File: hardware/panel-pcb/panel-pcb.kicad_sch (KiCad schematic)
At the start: 0 parts

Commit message: Panel PCB schematic: RP2040 core, flash, USB-C, power-in, RS-485
- RP2040 core: decoupling, ADC_AVDD filter, crystal, RUN, TESTEN, SWD header,
  values sourced from TI's official RP2040 hardware design guide
- W25Q32JV flash with BOOTSEL pushbutton (button instead of the guide's jumper,
  matching Pico's approach)
- USB-C connector (16-pin USB2.0-only), CC pull-downs, D+/D- series resistors,
  plus a VBUS/12V power-OR so the panel can be flashed and bench-tested over
  USB alone with 12V absent
- Power-in: 12V bus connectors, AMS1117-5.0 -> AMS1117-3.3 LDO cascade
- RS-485: THVD1419 transceiver, bused IN/OUT connectors, DPDT slide switch for
  termination (one pole gates the 120 ohm resistor, the other reports switch
  state to the RP2040 so termination state is always known)
- 3-bit player/pad ID DIP switch added to the master MCU spec, replacing
  stock SMX's jumper-based P1/P2 selection
- Panel PCB physical measurements replaced with real caliper measurements
  (mounting holes, LED lattice pitch, connector positions, board outline)
  from a pulled Gen5 panel, superseding the earlier photo-based estimates
- Preferred USB-C mounting style set to vertical DIP through-hole
- Reference photos of the stock panel PCB added under images/
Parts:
- added C1, C2: 15pF, Capacitor_SMD:C_0603_1608Metric, symbol Device:C
- added C10, C11, C12, C13, C15, C20, C5, C6, C7, C8, C9: 100nF, Capacitor_SMD:C_0603_1608Metric, symbol Device:C
- added C14, C4: 1uF, Capacitor_SMD:C_0603_1608Metric, symbol Device:C
- added C16, C18: 10uF, Capacitor_THT:CP_Radial_D6.3mm_P2.50mm, symbol Device:C
- added C17, C19: 22uF, Capacitor_THT:CP_Radial_D6.3mm_P2.50mm, symbol Device:C
- added C3: 2.2uF, Capacitor_SMD:C_0603_1608Metric, symbol Device:C
- added D1, D2: Schottky, Diode_SMD:D_SOD-123, symbol Device:D_Schottky
- added J1: SWD, Connector_PinHeader_2.54mm:PinHeader_1x03_P2.54mm_Vertical, symbol Connector_Generic:Conn_01x03
- added J2: USB_C_Receptacle_USB2.0_16P, symbol Connector:USB_C_Receptacle_USB2.0_16P
- added J3: 12V_IN, symbol Connector_Generic:Conn_01x02
- added J4: 12V_OUT, symbol Connector_Generic:Conn_01x02
- added J5: RS-485 IN, symbol Connector_Generic:Conn_01x03
- added J6: RS-485 OUT, symbol Connector_Generic:Conn_01x03
- added R1: 201R 1%, Resistor_SMD:R_0603_1608Metric, symbol Device:R
- added R10: 120, Resistor_SMD:R_0603_1608Metric, symbol Device:R
- added R2: 10k, Resistor_SMD:R_0603_1608Metric, symbol Device:R
- added R3: 1k 1%, Resistor_SMD:R_0603_1608Metric, symbol Device:R
- added R4: 1k, Resistor_SMD:R_0603_1608Metric, symbol Device:R
- added R5: 10k DNF, Resistor_SMD:R_0603_1608Metric, symbol Device:R
- added R6, R7: 27R 1%, Resistor_SMD:R_0603_1608Metric, symbol Device:R
- added R8, R9: 5.1k, Resistor_SMD:R_0603_1608Metric, symbol Device:R
- added SW1: BOOTSEL, Button_Switch_SMD:SW_SPST_B3U-1000P, symbol Switch:SW_Push
- added SW2: RS-485 Termination, symbol Switch:SW_Slide_DPDT
- added TP1: RUN, TestPoint:TestPoint_Pad_1.5x1.5mm, symbol Connector:TestPoint
- added U1: RP2040, Package_DFN_QFN:QFN-56-1EP_7x7mm_P0.4mm_EP3.2x3.2mm, symbol MCU_RaspberryPi:RP2040
- added U2: W25Q32JV, Package_SO:SOIC-8_5.3x5.3mm_P1.27mm, symbol Memory_Flash:W25Q32JVSS
- added U3: AMS1117-5.0, Package_TO_SOT_SMD:SOT-223-3_TabPin2, symbol Regulator_Linear:AMS1117-5.0
- added U4: AMS1117-3.3, Package_TO_SOT_SMD:SOT-223-3_TabPin2, symbol Regulator_Linear:AMS1117-3.3
- added U5: THVD1419, Package_SO:SOIC-8_3.9x4.9mm_P1.27mm, symbol Interface_UART:THVD1420D
- added X1: 12MHz, Crystal:Crystal_SMD_3225-4Pin_3.2x2.5mm, symbol Device:Crystal_GND24
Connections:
- new net: C2.1, R3.1, X1.3
- new net: J1.3 (Pin_3), U1.24 (SWCLK)
- new net: J1.1 (Pin_1), U1.25 (SWDIO)
- new net: R2.2, TP1.1, U1.26 (RUN)
- new net: C3.2, R1.2, U1.43 (ADC_AVDD)
- new net: R7.2, U1.46 (USB_DM)
- new net: R6.1, U1.47 (USB_DP)
- new net: J2.B5 (CC2), R9.1
- new net: J2.A5 (CC1), R8.2
- new net: C17.1, D2.2 (A), U3.2 (VO)
- new net: R10.2, SW2.1 (A)
- new net +1.1V: C12.1, C13.1, C4.1, U1.23 (DVDD), U1.45 (VREG_VOUT), U1.50 (DVDD)
- new net +12.0V: C16.1, J3.1 (Pin_1), J4.1 (Pin_1), U3.3 (VI)
- new net +3V3: C10.1, C11.1, C14.2, C15.1, C19.1, C20.1, C5.1, C6.1, C7.1, C8.1, C9.1, R1.1, R2.1, R5.1, U1.1 (IOVDD), U1.10 (IOVDD), U1.22 (IOVDD), U1.33 (IOVDD), U1.42 (IOVDD), U1.44 (VREG_VIN), U1.48 (USB_VDD), U1.49 (IOVDD), U2.8 (VCC), U4.2 (VO), U5.8 (VCC)
- new net +5.0V: C18.1, D1.1 (K), D2.1 (K), U4.3 (VI)
- new net GND: C1.2, C10.2, C11.2, C12.2, C13.2, C14.1, C15.2, C16.2, C17.2, C18.2, C19.2, C2.2, C20.2, C3.1, C4.2, C5.2, C6.2, C7.2, C8.2, C9.2, J1.2 (Pin_2), J2.A1 (GND), J2.A12 (GND), J2.B1 (GND), J2.B12 (GND), J2.SH (SHIELD), J3.2 (Pin_2), J4.2 (Pin_2), R8.1, R9.2, SW1.2, SW2.6 (C), U1.19 (TESTEN), U1.57 (GND), U2.4 (GND), U3.1 (GND), U4.1 (GND), U5.5 (GND), X1.2 (G), X1.4 (G)
- new net GPIO0: U1.2 (GPIO0), U5.4 (DI)
- new net GPIO1: U1.3 (GPIO1), U5.1 (RO)
- new net GPIO10: SW2.5 (B), U1.13 (GPIO10)
- new net GPIO11: U1.14 (GPIO11)
- new net GPIO12: U1.15 (GPIO12)
- new net GPIO13: U1.16 (GPIO13)
- new net GPIO14: U1.17 (GPIO14)
- new net GPIO15: U1.18 (GPIO15)
- new net GPIO16: U1.27 (GPIO16)
- new net GPIO17: U1.28 (GPIO17)
- new net GPIO18: U1.29 (GPIO18)
- new net GPIO19: U1.30 (GPIO19)
- new net GPIO2: U1.4 (GPIO2), U5.2 (~{RE}), U5.3 (DE)
- new net GPIO20: U1.31 (GPIO20)
- new net GPIO21: U1.32 (GPIO21)
- new net GPIO22: U1.34 (GPIO22)
- new net GPIO23: U1.35 (GPIO23)
- new net GPIO24: U1.36 (GPIO24)
- new net GPIO25: U1.37 (GPIO25)
- new net GPIO26/ADC0: U1.38 (GPIO26/ADC0)
- new net GPIO27/ADC1: U1.39 (GPIO27/ADC1)
- new net GPIO28/ADC2: U1.40 (GPIO28/ADC2)
- new net GPIO29/ADC3: U1.41 (GPIO29/ADC3)
- new net GPIO3: U1.5 (GPIO3)
- new net GPIO4: U1.6 (GPIO4)
- new net GPIO5: U1.7 (GPIO5)
- new net GPIO6: U1.8 (GPIO6)
- new net GPIO7: U1.9 (GPIO7)
- new net GPIO8: U1.11 (GPIO8)
- new net GPIO9: U1.12 (GPIO9)
- new net QSPI_SCLK: U1.52 (QSPI_SCLK), U2.6 (CLK)
- new net QSPI_SD0: U1.53 (QSPI_SD0), U2.5 (DI/IO_{0})
- new net QSPI_SD1: U1.55 (QSPI_SD1), U2.2 (DO/IO_{1})
- new net QSPI_SD2: U1.54 (QSPI_SD2), U2.3 (~{WP}/IO_{2})
- new net QSPI_SD3: U1.51 (QSPI_SD3), U2.7 (~{HOLD}/~{RESET}/IO_{3})
- new net QSPI_SS: R4.2, R5.2, U1.56 (~{QSPI_SS}), U2.1 (~{CS})
- new net RS485_A: J5.1 (Pin_1), J6.1 (Pin_1), SW2.2 (B), U5.6 (A)
- new net RS485_B: J5.2 (Pin_2), J6.2 (Pin_2), R10.1, U5.7 (B)
- new net USB_BOOT: R4.1, SW1.1
- new net USB_DM: J2.A7 (D-), J2.B7 (D-), R7.1
- new net USB_DP: J2.A6 (D+), J2.B6 (D+), R6.2
- new net VBUS: D1.2 (A), J2.A4 (VBUS), J2.A9 (VBUS), J2.B4 (VBUS), J2.B9 (VBUS)
- new net XIN: C1.1, U1.20 (XIN), X1.1
- new net XOUT: R3.2, U1.21 (XOUT)
- no-connect marks 0 -> 6
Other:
- note added: "12v Power"
- note added: "3v3 Power"
- note added: "5v Power"
- note added: "Buttons"
- note added: "Close to ADC_AVDD pin"
- note added: "Each close to a DVDD pin"
- note added: "Each close to an IOVDD pin"
- note added: "Microcontroller"
- note added: "QSPI Flash"
- note added: "RS-485"
- note added: "USB"

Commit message: Panel PCB schematic complete: FSR, LED chain, INT, ID DIP + doc updates
- FSR inputs x4 (J7-J10, 10k dividers, 10nF C0G ADC caps)
- LED chain: 25x WS2815 + SN74AHCT125 shifter, GPIO3 debug LED (optional populate)
- WS2815 per-LED 100nF corrected to VCC->GND per datasheet (BOM.md note fixed)
- INT out (100R series + single-pos terminal), 4-pos panel ID DIP
- Spare shifter gates: inputs + ~OE grounded, outputs no-connect
- Debug press LED gated to diagnostic modes 9-13 (docs/PANEL_CONFIG.md)

ERC clean, netlist-verified pin-exact (~330 parts).
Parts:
- added C21, C22, C23, C24: 10nF C0G, symbol Device:C
- added C25, C26, C27, C28, C29, C30, C31, C32, C33, C34, C35, C36, C37, C38, C39, C40, C41, C42, C43, C44, C45, C46, C47, C48, C49, C50: 100nF, symbol Device:C
- added D10, D11, D12, D13, D14, D15, D16, D17, D18, D19, D20, D21, D22, D23, D24, D25, D26, D27, D3, D4, D5, D6, D7, D8, D9: WS2815, symbol LED:WS2813
- added D28: DEBUG, symbol Device:LED
- added J10: FSR West, symbol Connector_Generic:Conn_01x02
- added J11: INT OUT, symbol Connector_Generic:Conn_01x01
- added J7: FSR North, symbol Connector_Generic:Conn_01x02
- added J8: FSR East, symbol Connector_Generic:Conn_01x02
- added J9: FSR South, symbol Connector_Generic:Conn_01x02
- added R11, R12, R13, R14: 10k, symbol Device:R
- added R15: 100R, symbol Device:R
- added R16: 330R, symbol Device:R
- added R17: 1k, symbol Device:R
- added SW3: PANEL_ID, symbol Switch:SW_DIP_x04
- added U6: SN74AHCT125, symbol 74xx:74AHCT125
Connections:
- net +12.0V: now also D10.2 (VDD), D11.2 (VDD), D12.2 (VDD), D13.2 (VDD), D14.2 (VDD), D15.2 (VDD), D16.2 (VDD), D17.2 (VDD), D18.2 (VDD), D19.2 (VDD), D20.2 (VDD), D21.2 (VDD), D22.2 (VDD), D23.2 (VDD), D24.2 (VDD), D25.2 (VDD), D26.2 (VDD), D27.2 (VDD), D3.2 (VDD), D4.2 (VDD), D5.2 (VDD), D6.2 (VDD), D7.2 (VDD), D8.2 (VDD), D9.2 (VDD)
- net +3V3: now also J10.2 (Pin_2), J7.2 (Pin_2), J8.2 (Pin_2), J9.2 (Pin_2)
- net +5.0V: now also C50.1, U6.14 (VCC)
- net GND: now also C21.2, C22.2, C23.2, C24.2, C25.2, C26.2, C27.2, C28.2, C29.2, C30.2, C31.2, C32.2, C33.2, C34.2, C35.2, C36.2, C37.2, C38.2, C39.2, C40.2, C41.2, C42.2, C43.2, C44.2, C45.2, C46.2, C47.2, C48.2, C49.2, C50.2, D10.5 (GND), D11.5 (GND), D12.5 (GND), D13.5 (GND), D14.5 (GND), D15.5 (GND), D16.5 (GND), D17.5 (GND), D18.5 (GND), D19.5 (GND), D20.5 (GND), D21.5 (GND), D22.5 (GND), D23.5 (GND), D24.5 (GND), D25.5 (GND), D26.5 (GND), D27.5 (GND), D28.1 (K), D3.5 (GND), D4.5 (GND), D5.5 (GND), D6.5 (GND), D7.5 (GND), D8.5 (GND), D9.5 (GND), R11.2, R12.2, R13.2, R14.2, SW3.5, SW3.6, SW3.7, SW3.8, U6.1, U6.10, U6.12, U6.13, U6.4, U6.5, U6.7 (GND), U6.9
- net GPIO16: now also U6.2
- net GPIO26/ADC0: now also C21.1, J7.1 (Pin_1), R11.1
- net GPIO27/ADC1: now also C22.1, J8.1 (Pin_1), R12.1
- net GPIO28/ADC2: now also C23.1, J9.1 (Pin_1), R13.1
- net GPIO29/ADC3: now also C24.1, J10.1 (Pin_1), R14.1
- net GPIO3: now also R17.1
- net GPIO5: now also R15.1
- net GPIO6: now also SW3.1
- net GPIO7: now also SW3.2
- net GPIO8: now also SW3.3
- net GPIO9: now also SW3.4
- new net: C44.1, D22.1 (VCC)
- new net: C41.1, D19.1 (VCC)
- new net: C28.1, D6.1 (VCC)
- new net: C32.1, D10.1 (VCC)
- new net: C39.1, D17.1 (VCC)
- new net: C35.1, D13.1 (VCC)
- new net: C36.1, D14.1 (VCC)
- new net: C25.1, D3.1 (VCC)
- new net: C42.1, D20.1 (VCC)
- new net: C40.1, D18.1 (VCC)
- new net: C37.1, D15.1 (VCC)
- new net: C48.1, D26.1 (VCC)
- new net: C43.1, D21.1 (VCC)
- new net: C31.1, D9.1 (VCC)
- new net: C26.1, D4.1 (VCC)
- new net: C30.1, D8.1 (VCC)
- new net: J11.1 (Pin_1), R15.2
- new net: C38.1, D16.1 (VCC)
- new net: R16.1, U6.3
- new net: C45.1, D23.1 (VCC)
- new net: C47.1, D25.1 (VCC)
- new net: C27.1, D5.1 (VCC)
- new net: C29.1, D7.1 (VCC)
- new net: C49.1, D27.1 (VCC)
- new net: D28.2 (A), R17.2
- new net: C34.1, D12.1 (VCC)
- new net: C46.1, D24.1 (VCC)
- new net: C33.1, D11.1 (VCC)
- new net LD0: D3.4 (DIN), D3.6 (BIN), D4.6 (BIN), R16.2
- new net LD1: D3.3 (DOUT), D4.4 (DIN), D5.6 (BIN)
- new net LD10: D12.3 (DOUT), D13.4 (DIN), D14.6 (BIN)
- new net LD11: D13.3 (DOUT), D14.4 (DIN), D15.6 (BIN)
- new net LD12: D14.3 (DOUT), D15.4 (DIN), D16.6 (BIN)
- new net LD13: D15.3 (DOUT), D16.4 (DIN), D17.6 (BIN)
- new net LD14: D16.3 (DOUT), D17.4 (DIN), D18.6 (BIN)
- new net LD15: D17.3 (DOUT), D18.4 (DIN), D19.6 (BIN)
- new net LD16: D18.3 (DOUT), D19.4 (DIN), D20.6 (BIN)
- new net LD17: D19.3 (DOUT), D20.4 (DIN), D21.6 (BIN)
- new net LD18: D20.3 (DOUT), D21.4 (DIN), D22.6 (BIN)
- new net LD19: D21.3 (DOUT), D22.4 (DIN), D23.6 (BIN)
- new net LD2: D4.3 (DOUT), D5.4 (DIN), D6.6 (BIN)
- new net LD20: D22.3 (DOUT), D23.4 (DIN), D24.6 (BIN)
- new net LD21: D23.3 (DOUT), D24.4 (DIN), D25.6 (BIN)
- new net LD22: D24.3 (DOUT), D25.4 (DIN), D26.6 (BIN)
- new net LD23: D25.3 (DOUT), D26.4 (DIN), D27.6 (BIN)
- new net LD24: D26.3 (DOUT), D27.4 (DIN)
- new net LD3: D5.3 (DOUT), D6.4 (DIN), D7.6 (BIN)
- new net LD4: D6.3 (DOUT), D7.4 (DIN), D8.6 (BIN)
- new net LD5: D7.3 (DOUT), D8.4 (DIN), D9.6 (BIN)
- new net LD6: D10.6 (BIN), D8.3 (DOUT), D9.4 (DIN)
- new net LD7: D10.4 (DIN), D11.6 (BIN), D9.3 (DOUT)
- new net LD8: D10.3 (DOUT), D11.4 (DIN), D12.6 (BIN)
- new net LD9: D11.3 (DOUT), D12.4 (DIN), D13.6 (BIN)
- no-connect marks 6 -> 10
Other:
- note added: "DIP Switch"
- note added: "FSRs"
- note added: "INT Out"
- note added: "LED Grid"
- moved on the sheet: C1, C2, R3, X1

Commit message: Schematic: GUI reorganization, re-annotate by position, 11 test points, normalization pass
- User reorganized layout + re-annotated all refs by sheet position
  (verified: connectivity identical via UUID-mapped netlist diff, ERC 0 errors)
- 10 new test points (TP2-TP11): rails, GND x2, UART TX/RX, RS-485 dir,
  LED data 3.3V/5V sides
- Normalization (133 property changes): cap dielectrics + voltage ratings
  (15pF C0G, 10nF C0G 50V, 100nF X7R 50V, LDO electrolytics 25V), FSR
  pull-downs 10k 1%, power-OR Schottkys -> 1N5819W, footprints for all
  passives/LEDs/JST-PH/Micro-Fit/DIP/SOIC-14
- Still TBD at sourcing: USB-C receptacle (J1), INT terminal (J9),
  DPDT slide (SW1) footprints
- Docs: re-annotation notice + current-ref table in PANEL_SCHEMATIC_PLAN,
  stale refs fixed in PANEL_CONFIG + layout notes
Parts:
- added TP10: +5.0V, TestPoint:TestPoint_Pad_1.5x1.5mm, symbol Connector:TestPoint
- added TP11: +3V3, TestPoint:TestPoint_Pad_1.5x1.5mm, symbol Connector:TestPoint
- added TP2, TP3: GND, TestPoint:TestPoint_Pad_1.5x1.5mm, symbol Connector:TestPoint
- added TP4: UART RX, TestPoint:TestPoint_Pad_1.5x1.5mm, symbol Connector:TestPoint
- added TP5: UART TX, TestPoint:TestPoint_Pad_1.5x1.5mm, symbol Connector:TestPoint
- added TP6: RS-485 DC, TestPoint:TestPoint_Pad_1.5x1.5mm, symbol Connector:TestPoint
- added TP7: LED Data 3.3V, TestPoint:TestPoint_Pad_1.5x1.5mm, symbol Connector:TestPoint
- added TP8: +12.0V, TestPoint:TestPoint_Pad_1.5x1.5mm, symbol Connector:TestPoint
- added TP9: LED Data 5.0V, TestPoint:TestPoint_Pad_1.5x1.5mm, symbol Connector:TestPoint
- C1: renamed from C11; value 100nF -> 100nF X7R 50V
- C10: renamed from C20; value 100nF -> 100nF X7R 50V
- C11: renamed from C5; value 100nF -> 100nF X7R 50V
- C12: renamed from C1; value 15pF -> 15pF C0G 50V
- C13: renamed from C12; value 100nF -> 100nF X7R 50V
- C14: renamed from C2; value 15pF -> 15pF C0G 50V
- C15: renamed from C13; value 100nF -> 100nF X7R 50V
- C16: renamed from C21; value 10nF C0G -> 10nF C0G 50V; footprint (none) -> Capacitor_SMD:C_0603_1608Metric
- C17: renamed from C23; value 10nF C0G -> 10nF C0G 50V; footprint (none) -> Capacitor_SMD:C_0603_1608Metric
- C18: renamed from C22; value 10nF C0G -> 10nF C0G 50V; footprint (none) -> Capacitor_SMD:C_0603_1608Metric
- C19: renamed from C24; value 10nF C0G -> 10nF C0G 50V; footprint (none) -> Capacitor_SMD:C_0603_1608Metric
- C2: renamed from C10; value 100nF -> 100nF X7R 50V
- C20: renamed from C15; value 100nF -> 100nF X7R 50V
- C21: renamed from C50; value 100nF -> 100nF X7R 50V; footprint (none) -> Capacitor_SMD:C_0603_1608Metric
- C22: renamed from C25; value 100nF -> 100nF X7R 50V; footprint (none) -> Capacitor_SMD:C_0603_1608Metric
- C23: renamed from C30; value 100nF -> 100nF X7R 50V; footprint (none) -> Capacitor_SMD:C_0603_1608Metric
- C24: renamed from C35; value 100nF -> 100nF X7R 50V; footprint (none) -> Capacitor_SMD:C_0603_1608Metric
- C25: renamed from C40; value 100nF -> 100nF X7R 50V; footprint (none) -> Capacitor_SMD:C_0603_1608Metric
- C26: renamed from C45; value 100nF -> 100nF X7R 50V; footprint (none) -> Capacitor_SMD:C_0603_1608Metric
- C27: renamed from C26; value 100nF -> 100nF X7R 50V; footprint (none) -> Capacitor_SMD:C_0603_1608Metric
- C28: renamed from C31; value 100nF -> 100nF X7R 50V; footprint (none) -> Capacitor_SMD:C_0603_1608Metric
- C29: renamed from C36; value 100nF -> 100nF X7R 50V; footprint (none) -> Capacitor_SMD:C_0603_1608Metric
- C3: renamed from C9; value 100nF -> 100nF X7R 50V
- C30: renamed from C41; value 100nF -> 100nF X7R 50V; footprint (none) -> Capacitor_SMD:C_0603_1608Metric
- C31: renamed from C46; value 100nF -> 100nF X7R 50V; footprint (none) -> Capacitor_SMD:C_0603_1608Metric
- C32: renamed from C27; value 100nF -> 100nF X7R 50V; footprint (none) -> Capacitor_SMD:C_0603_1608Metric
- C33: renamed from C32; value 100nF -> 100nF X7R 50V; footprint (none) -> Capacitor_SMD:C_0603_1608Metric
- C34: renamed from C37; value 100nF -> 100nF X7R 50V; footprint (none) -> Capacitor_SMD:C_0603_1608Metric
- C35: renamed from C42; value 100nF -> 100nF X7R 50V; footprint (none) -> Capacitor_SMD:C_0603_1608Metric
- C36: renamed from C47; value 100nF -> 100nF X7R 50V; footprint (none) -> Capacitor_SMD:C_0603_1608Metric
- C37: renamed from C16; value 10uF -> 10uF elec 25V
- C38: renamed from C17; value 22uF -> 22uF elec 25V
- C39: renamed from C28; value 100nF -> 100nF X7R 50V; footprint (none) -> Capacitor_SMD:C_0603_1608Metric
- C4: renamed from C3; value 2.2uF -> 2.2uF X5R 16V
- C40: renamed from C33; value 100nF -> 100nF X7R 50V; footprint (none) -> Capacitor_SMD:C_0603_1608Metric
- C41: renamed from C38; value 100nF -> 100nF X7R 50V; footprint (none) -> Capacitor_SMD:C_0603_1608Metric
- C42: renamed from C43; value 100nF -> 100nF X7R 50V; footprint (none) -> Capacitor_SMD:C_0603_1608Metric
- C43: renamed from C48; value 100nF -> 100nF X7R 50V; footprint (none) -> Capacitor_SMD:C_0603_1608Metric
- C44: renamed from C18; value 10uF -> 10uF elec 25V
- C45: renamed from C29; value 100nF -> 100nF X7R 50V; footprint (none) -> Capacitor_SMD:C_0603_1608Metric
- C46: renamed from C34; value 100nF -> 100nF X7R 50V; footprint (none) -> Capacitor_SMD:C_0603_1608Metric
- C47: renamed from C39; value 100nF -> 100nF X7R 50V; footprint (none) -> Capacitor_SMD:C_0603_1608Metric
- C48: renamed from C44; value 100nF -> 100nF X7R 50V; footprint (none) -> Capacitor_SMD:C_0603_1608Metric
- C49: value 100nF -> 100nF X7R 50V; footprint (none) -> Capacitor_SMD:C_0603_1608Metric
- C5: renamed from C8; value 100nF -> 100nF X7R 50V
- C50: renamed from C19; value 22uF -> 22uF elec 25V
- C6: renamed from C14; value 1uF -> 1uF X5R 16V
- C7: value 100nF -> 100nF X7R 50V
- C8: renamed from C6; value 100nF -> 100nF X7R 50V
- C9: renamed from C4; value 1uF -> 1uF X5R 16V
- D1: renamed from D28; footprint (none) -> LED_SMD:LED_0603_1608Metric
- D10: renamed from D19; footprint (none) -> LED_SMD:LED_WS2812B_PLCC4_5.0x5.0mm_P3.2mm
- D11: renamed from D24; footprint (none) -> LED_SMD:LED_WS2812B_PLCC4_5.0x5.0mm_P3.2mm
- D12: renamed from D1; value Schottky -> 1N5819W
- D13: renamed from D5; footprint (none) -> LED_SMD:LED_WS2812B_PLCC4_5.0x5.0mm_P3.2mm
- D14: renamed from D10; footprint (none) -> LED_SMD:LED_WS2812B_PLCC4_5.0x5.0mm_P3.2mm
- D15, D21: footprint (none) -> LED_SMD:LED_WS2812B_PLCC4_5.0x5.0mm_P3.2mm
- D16: renamed from D20; footprint (none) -> LED_SMD:LED_WS2812B_PLCC4_5.0x5.0mm_P3.2mm
- D17: renamed from D25; footprint (none) -> LED_SMD:LED_WS2812B_PLCC4_5.0x5.0mm_P3.2mm
- D18: renamed from D6; footprint (none) -> LED_SMD:LED_WS2812B_PLCC4_5.0x5.0mm_P3.2mm
- D19: renamed from D11; footprint (none) -> LED_SMD:LED_WS2812B_PLCC4_5.0x5.0mm_P3.2mm
- D2: renamed from D3; footprint (none) -> LED_SMD:LED_WS2812B_PLCC4_5.0x5.0mm_P3.2mm
- D20: renamed from D16; footprint (none) -> LED_SMD:LED_WS2812B_PLCC4_5.0x5.0mm_P3.2mm
- D22: renamed from D26; footprint (none) -> LED_SMD:LED_WS2812B_PLCC4_5.0x5.0mm_P3.2mm
- D23: renamed from D2; value Schottky -> 1N5819W
- D24: renamed from D7; footprint (none) -> LED_SMD:LED_WS2812B_PLCC4_5.0x5.0mm_P3.2mm
- D25: renamed from D12; footprint (none) -> LED_SMD:LED_WS2812B_PLCC4_5.0x5.0mm_P3.2mm
- D26: renamed from D17; footprint (none) -> LED_SMD:LED_WS2812B_PLCC4_5.0x5.0mm_P3.2mm
- D27: renamed from D22; footprint (none) -> LED_SMD:LED_WS2812B_PLCC4_5.0x5.0mm_P3.2mm
- D28: renamed from D27; footprint (none) -> LED_SMD:LED_WS2812B_PLCC4_5.0x5.0mm_P3.2mm
- D3: renamed from D8; footprint (none) -> LED_SMD:LED_WS2812B_PLCC4_5.0x5.0mm_P3.2mm
- D4: renamed from D13; footprint (none) -> LED_SMD:LED_WS2812B_PLCC4_5.0x5.0mm_P3.2mm
- D5: renamed from D18; footprint (none) -> LED_SMD:LED_WS2812B_PLCC4_5.0x5.0mm_P3.2mm
- D6: renamed from D23; footprint (none) -> LED_SMD:LED_WS2812B_PLCC4_5.0x5.0mm_P3.2mm
- D7: renamed from D4; footprint (none) -> LED_SMD:LED_WS2812B_PLCC4_5.0x5.0mm_P3.2mm
- D8: renamed from D9; footprint (none) -> LED_SMD:LED_WS2812B_PLCC4_5.0x5.0mm_P3.2mm
- D9: renamed from D14; footprint (none) -> LED_SMD:LED_WS2812B_PLCC4_5.0x5.0mm_P3.2mm
- J10: renamed from J6; footprint (none) -> Connector_Molex:Molex_Micro-Fit_3.0_43650-0310_1x03-1MP_P3.00mm_Horizontal
- J11: renamed from J4; footprint (none) -> Connector_Molex:Molex_Micro-Fit_3.0_43650-0210_1x02-1MP_P3.00mm_Horizontal
- J3: renamed from J7; footprint (none) -> Connector_JST:JST_PH_B2B-PH-K_1x02_P2.00mm_Vertical
- J4: renamed from J8; footprint (none) -> Connector_JST:JST_PH_B2B-PH-K_1x02_P2.00mm_Vertical
- J5: renamed from J3; footprint (none) -> Connector_Molex:Molex_Micro-Fit_3.0_43650-0210_1x02-1MP_P3.00mm_Horizontal
- J6: renamed from J9; footprint (none) -> Connector_JST:JST_PH_B2B-PH-K_1x02_P2.00mm_Vertical
- J7: renamed from J10; footprint (none) -> Connector_JST:JST_PH_B2B-PH-K_1x02_P2.00mm_Vertical
- J8: renamed from J5; footprint (none) -> Connector_Molex:Molex_Micro-Fit_3.0_43650-0310_1x03-1MP_P3.00mm_Horizontal
- R10: renamed from R12; value 10k -> 10k 1%; footprint (none) -> Resistor_SMD:R_0603_1608Metric
- R11: renamed from R14; value 10k -> 10k 1%; footprint (none) -> Resistor_SMD:R_0603_1608Metric
- R15: renamed from R17; footprint (none) -> Resistor_SMD:R_0603_1608Metric
- R16: footprint (none) -> Resistor_SMD:R_0603_1608Metric
- R17: renamed from R15; footprint (none) -> Resistor_SMD:R_0603_1608Metric
- R8: renamed from R11; value 10k -> 10k 1%; footprint (none) -> Resistor_SMD:R_0603_1608Metric
- R9: renamed from R13; value 10k -> 10k 1%; footprint (none) -> Resistor_SMD:R_0603_1608Metric
- SW1: renamed from SW3; footprint (none) -> Button_Switch_THT:SW_DIP_SPSTx04_Slide_9.78x12.34mm_W7.62mm_P2.54mm
- U4: renamed from U6; footprint (none) -> Package_SO:SOIC-14_3.9x8.7mm_P1.27mm
- renumbered J2 to J1, J1 to J2, J11 to J9, R2 to R1, R5 to R12, R8 to R13, R9 to R14, R10 to R2, R7 to R3, R6 to R4, R1 to R5, R3 to R6, R4 to R7, SW1 to SW2, SW2 to SW3, U5 to U2, U2 to U3, U3 to U5, U4 to U6
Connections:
- net +12.0V: now also TP8.1
- net +3V3: now also TP11.1
- net +5.0V: now also TP10.1
- net GND: now also TP2.1, TP3.1
- net GPIO0: now also TP5.1
- net GPIO1: now also TP4.1
- net GPIO16: now also TP7.1
- net GPIO2: now also TP6.1
- net SWCLK: now reaches J2.3 (Pin_3), U1.24 (SWCLK)
- net SWDIO: now reaches J2.1 (Pin_1), U1.25 (SWDIO)
- net LD0: no longer names the net of D2.4 (DIN), D2.6 (BIN), D7.6 (BIN), R16.2
- net LD0: now also TP9.1
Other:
- note added: "Buttons & Switches"
- note added: "Force-Sensitive Resistors (FSRs)"
- note added: "Inputs"
- note added: "LED Grid & Logic Shifter"
- note added: "Outputs"
- note added: "Power Management"
- note added: "RS-485 Receive & Transmit"
- note removed: "12v Power"
- note removed: "3v3 Power"
- note removed: "5v Power"
- note removed: "Buttons"
- note removed: "DIP Switch"
- note removed: "FSRs"
- note removed: "INT Out"
- note removed: "LED Grid"
- note removed: "RS-485"
- moved on the sheet: C10, C16, C17, C18, C19, C20, C21, C37, C38, C44, C50, D1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

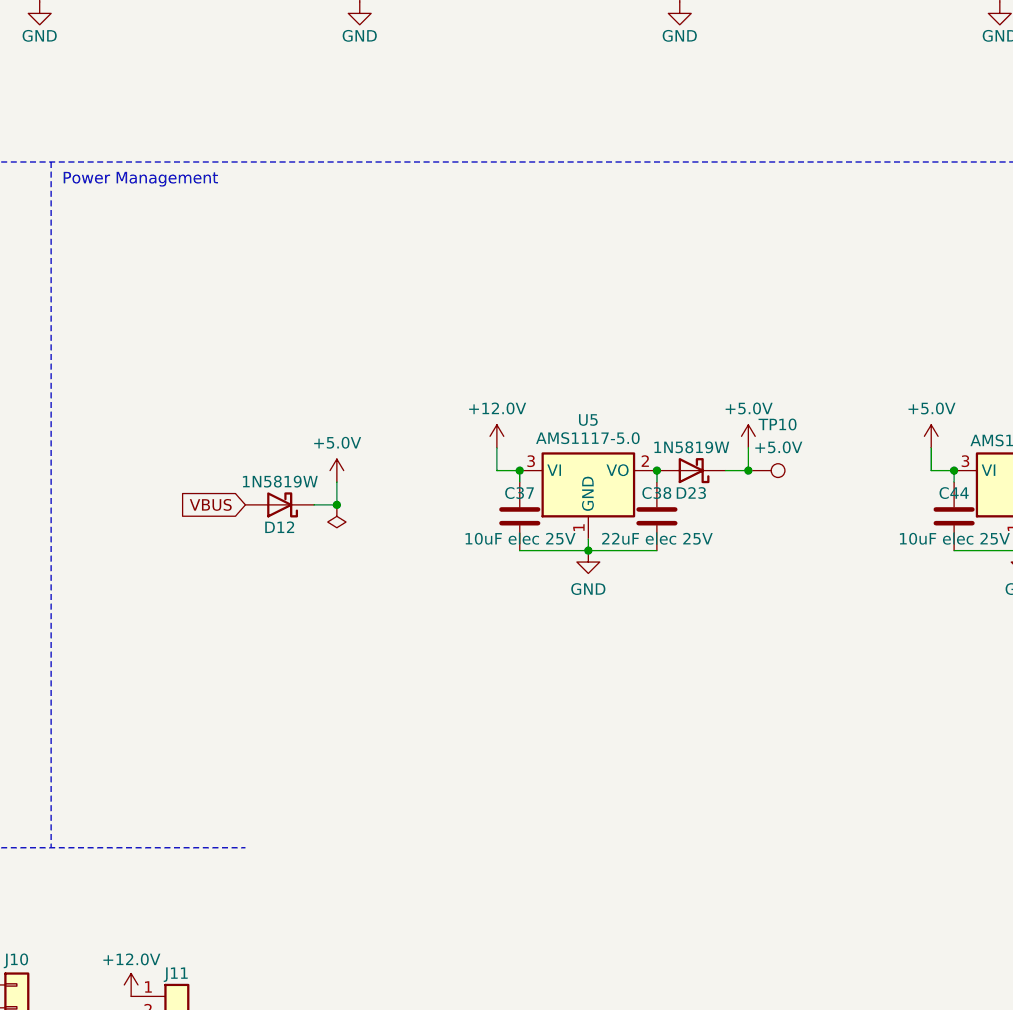
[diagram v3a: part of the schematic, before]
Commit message: Add C51 470uF 12V bulk cap for LED load steps (user-placed, verified); fix inherited description
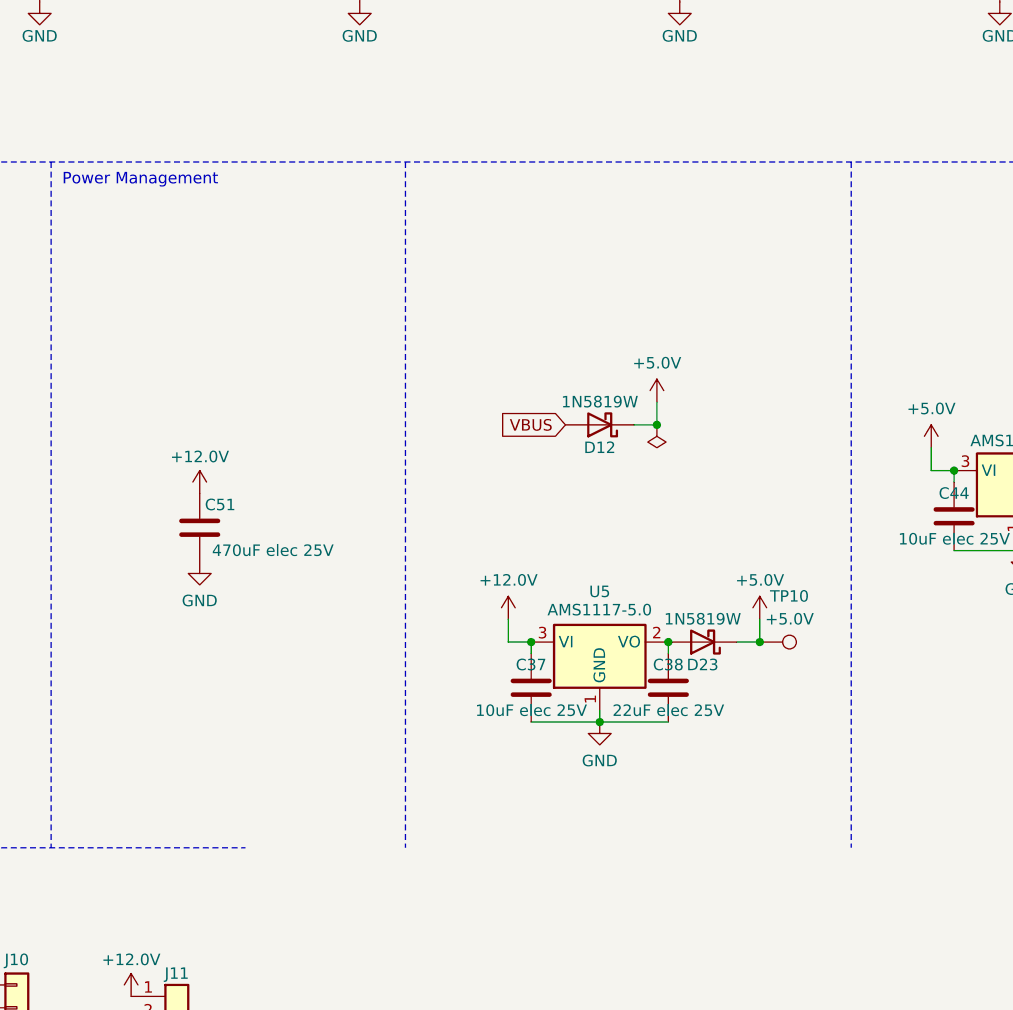
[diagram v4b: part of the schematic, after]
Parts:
- added C51: 470uF elec 25V, Capacitor_THT:CP_Radial_D6.3mm_P2.50mm, symbol Device:C
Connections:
- net +12.0V: now also C51.1
- net GND: now also C51.2
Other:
- moved on the sheet: C37, C38, D12, D23, TP10, U5
